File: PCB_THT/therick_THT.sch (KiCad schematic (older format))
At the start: 107 parts, among them J1 TYPE-C-31-M12_13, J2 4PIN, K1 KEYSW, K10 KEYSW, K11 KEYSW, K12 KEYSW, K13 KEYSW, K14 KEYSW, K15 KEYSW, K16 KEYSW, K17 KEYSW, K18 KEYSW, K19 KEYSW, K2 KEYSW, K20 KEYSW, K21 KEYSW, K22 KEYSW, K23 KEYSW, K24 KEYSW, K25 KEYSW, K26 KEYSW, K27 KEYSW, K28 KEYSW, K29 KEYSW, K3 KEYSW, K30 KEYSW, K31 KEYSW, K32 KEYSW, K33 KEYSW, K34 KEYSW, K35 KEYSW, K36 KEYSW, K37 KEYSW, K38 KEYSW, K39 KEYSW, K4 KEYSW, K40 KEYSW, K41 KEYSW, K42 KEYSW, K43 KEYSW, K44 KEYSW, K45 KEYSW, K46 KEYSW, K47 KEYSW, K48 KEYSW, K5 KEYSW, K6 KEYSW, K7 KEYSW, K8 KEYSW, K9 KEYSW, SW1 SW_PUSH, U1 ProMicro, U2 HOLE

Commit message: Slimmed down USB port
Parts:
- J1: footprint acheron_Connectors:TYPE-C-31-M-12 -> random-keyboard-parts:TYPE-C-31-M-12
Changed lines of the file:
@@
 F 0 "J1" H 1857 6617 50  0000 C CNN
 F 1 "TYPE-C-31-M12_13" H 1857 6526 50  0000 C CNN
-F 2 "acheron_Connectors:TYPE-C-31-M-12" V 1250 5250 50  0001 C CNN
+F 2 "random-keyboard-parts:TYPE-C-31-M-12" V 1250 5250 50  0001 C CNN
 F 3 "https://www.usb.org/sites/default/files/documents/usb_type-c.zip" H 1950 5250 50  0001 C CNN
 	1    1750 5200

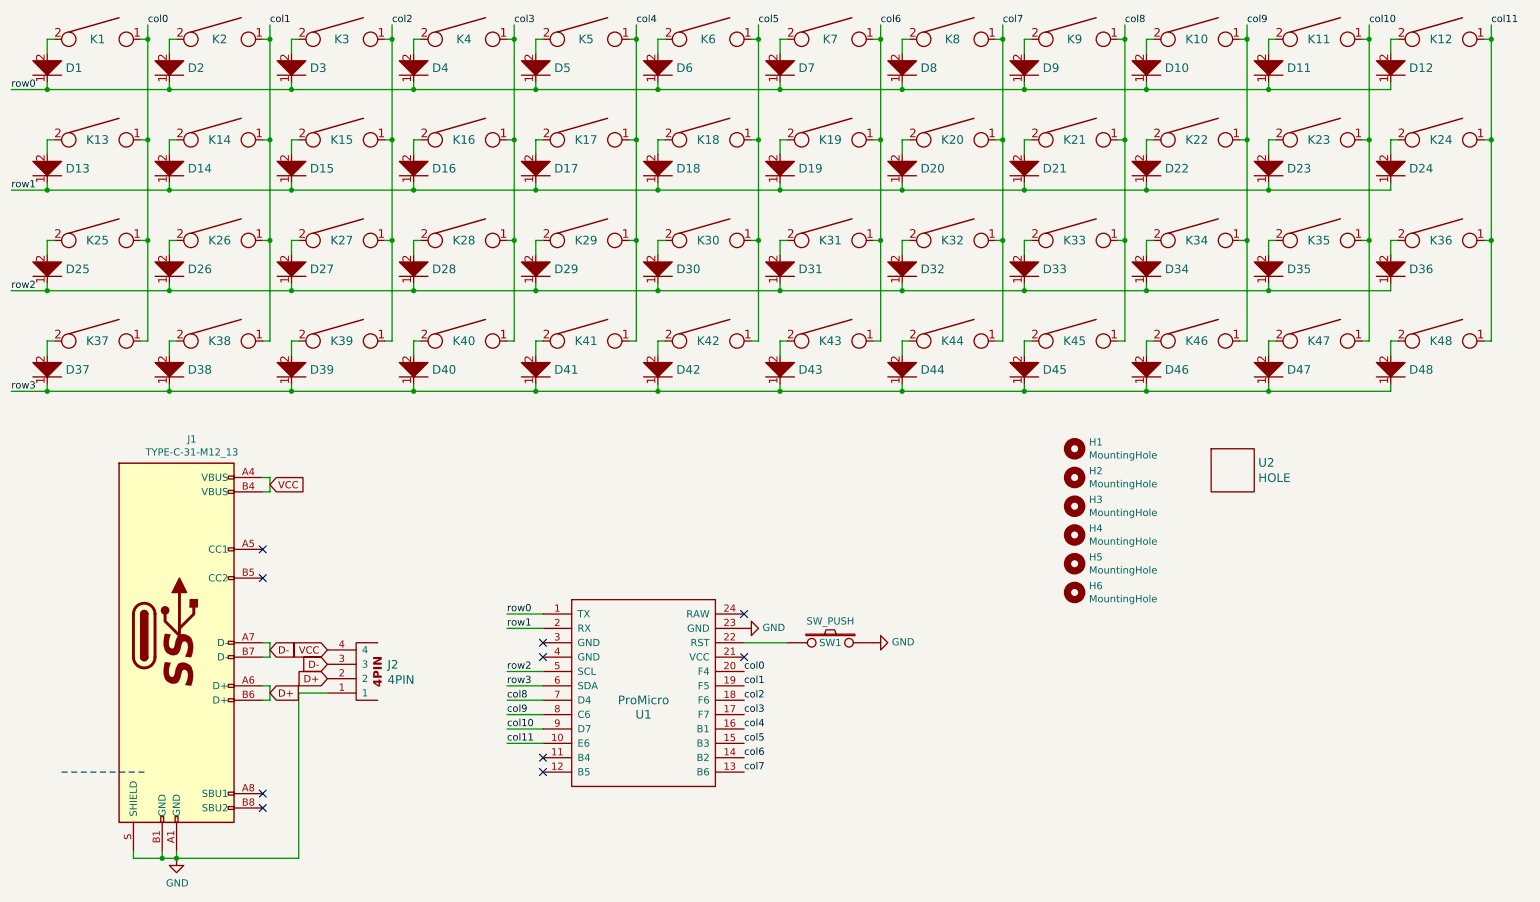
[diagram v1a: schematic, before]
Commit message: Removed Type C Connector
Only uses a Pro Micro/Elite C now
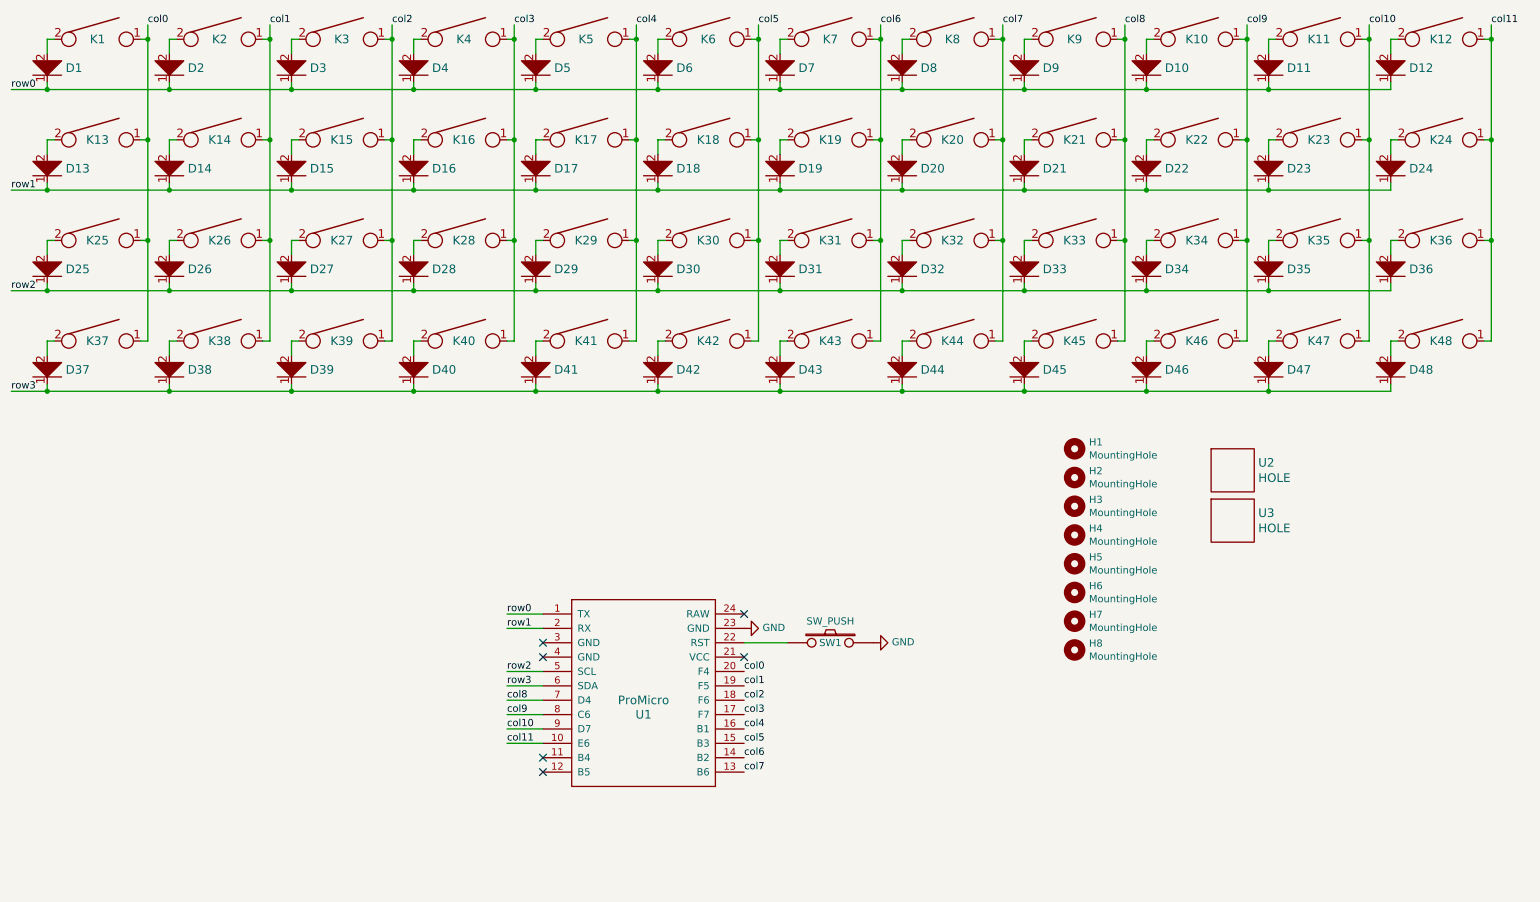
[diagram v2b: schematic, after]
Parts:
- removed J1: TYPE-C-31-M12_13, random-keyboard-parts:TYPE-C-31-M-12, symbol acheronSymbols:TYPE-C-31-M12_13
- removed J2: 4PIN, acheron_Connectors:PinHeader_1x4_P2.54mm_Vertical_B_mask, symbol component:4PIN
- added H7, H8: MountingHole, random-keyboard-parts:Generic-Mounthole, symbol Mechanical:MountingHole
- added U3: HOLE, Artwork:THERICK, symbol lets_split-cache:HOLE
- K1, K10, K11, K12, K13, K14, K15, K16, K17, K18, K19, K2, K20, K21, K22, K23, K24, K25, K26, K27, K28, K29, K3, K30, K31, K32, K33, K34, K35, K36, K37, K38, K39, K4, K40, K41, K42, K43, K44, K45, K46, K47, K48, K5, K6, K7, K8, K9: footprint MX_Only:MXOnly-1U-NoLED -> Keeb_footprints:MX100
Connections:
- no-connect marks 10 -> 6
